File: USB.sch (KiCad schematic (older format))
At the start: 7 parts

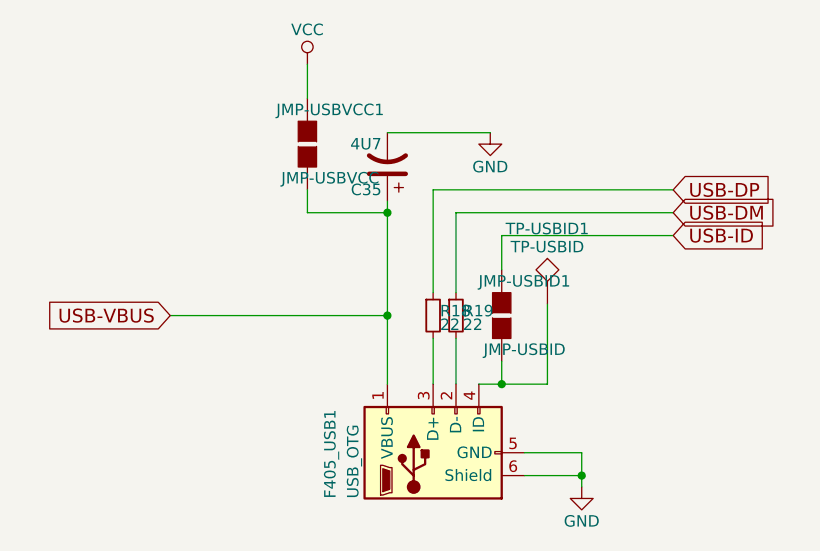
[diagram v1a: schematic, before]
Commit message: zone movement + routing of all circuits
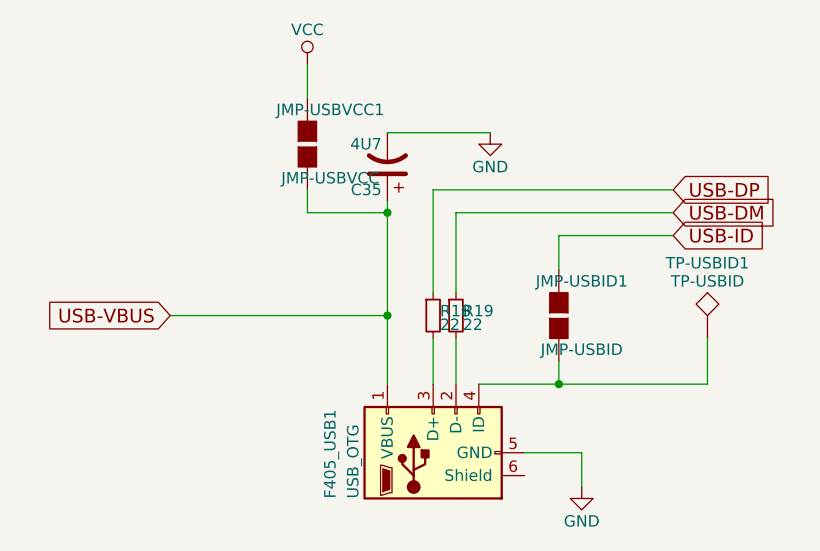
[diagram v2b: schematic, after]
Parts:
- C35: footprint (none) -> Capacitors_SMD:C_0805
- F405_USB1: footprint (none) -> gsg-modules:USB-MICROB-FCI-10103592-EXT
- JMP-USBID1, JMP-USBVCC1: footprint Connectors:GS2 -> Connect:GS2
- R18, R19: footprint (none) -> Resistors_SMD:R_0603
- TP-USBID1: footprint (none) -> Measurement_Points:Measurement_Point_Round-SMD-Pad_Small
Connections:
- net GND: no longer F405_USB1.6 (Shield)
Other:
- moved on the sheet: JMP-USBID1, TP-USBID1
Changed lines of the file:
@@
 EESchema Schematic File Version 2
 LIBS:power
-LIBS:device
 LIBS:transistors
 LIBS:conn
@@
 LIBS:sensors
 LIBS:dc-dc
+LIBS:device
 LIBS:dc26-cache
 EELAYER 25 0
@@
 $Descr A4 11693 8268
 encoding utf-8
-Sheet 5 6
+Sheet 4 6
 Title ""
 Date ""
@@
 F 0 "F405_USB1" H 5650 4750 50  0000 L CNN
 F 1 "USB_OTG" H 5650 4650 50  0000 L CNN
-F 2 "" H 6000 4250 50  0001 C CNN
+F 2 "gsg-modules:USB-MICROB-FCI-10103592-EXT" H 6000 4250 50  0001 C CNN
 F 3 "" H 6000 4250 50  0001 C CNN
 	1    5850 4300
@@
 F 0 "R18" H 5880 3720 50  0000 L CNN
 F 1 "22" H 5880 3660 50  0000 L CNN
-F 2 "" H 5850 3700 50  0001 C CNN
+F 2 "Resistors_SMD:R_0603" H 5850 3700 50  0001 C CNN
 F 3 "" H 5850 3700 50  0001 C CNN
 	1    5850 3700
@@
 F 0 "R19" H 5980 3720 50  0000 L CNN
 F 1 "22" H 5980 3660 50  0000 L CNN
-F 2 "" H 5950 3700 50  0001 C CNN
+F 2 "Resistors_SMD:R_0603" H 5950 3700 50  0001 C CNN
 F 3 "" H 5950 3700 50  0001 C CNN
 	1    5950 3700
@@
 F 0 "C35" H 5675 3150 50  0000 L CNN
 F 1 "4U7" H 5675 2950 50  0000 L CNN
-F 2 "" H 5650 3050 50  0001 C CNN
+F 2 "Capacitors_SMD:C_0805" H 5650 3050 50  0001 C CNN
 F 3 "" H 5650 3050 50  0001 C CNN
 	1    5650 3050
@@
 $EndComp
 $Comp
-L GND #PWR1248
+L GND #PWR043
 U 1 1 5B312B57
 P 6100 2900
-F 0 "#PWR1248" H 6100 2650 50  0001 C CNN
+F 0 "#PWR043" H 6100 2650 50  0001 C CNN
 F 1 "GND" H 6100 2750 50  0000 C CNN
 F 2 "" H 6100 2900 50  0001 C CNN
@@
 $EndComp
 $Comp
-L GND #PWR1249
+L GND #PWR044
 U 1 1 5B312B5D
 P 6500 4450
-F 0 "#PWR1249" H 6500 4200 50  0001 C CNN
+F 0 "#PWR044" H 6500 4200 50  0001 C CNN
 F 1 "GND" H 6500 4300 50  0000 C CNN
 F 2 "" H 6500 4450 50  0001 C CNN
@@
 L TEST TP-USBID1
 U 1 1 5B312B63
-P 6350 3650
-F 0 "TP-USBID1" H 6350 3950 50  0000 C BNN
-F 1 "TP-USBID" H 6350 3900 50  0000 C CNN
-F 2 "" H 6350 3650 50  0001 C CNN
-F 3 "" H 6350 3650 50  0001 C CNN
-	1    6350 3650
+P 7050 3800
+F 0 "TP-USBID1" H 7050 4100 50  0000 C BNN
+F 1 "TP-USBID" H 7050 4050 50  0000 C CNN
+F 2 "Measurement_Points:Measurement_Point_Round-SMD-Pad_Small" H 7050 3800 50  0001 C CNN
+F 3 "" H 7050 3800 50  0001 C CNN
+	1    7050 3800
 	1    0    0    -1
 $EndComp
@@
 L GS2 JMP-USBID1
 U 1 1 5B312B6A
-P 6150 3700
-F 0 "JMP-USBID1" H 6250 3850 50  0000 C CNN
-F 1 "JMP-USBID" H 6250 3551 50  0000 C CNN
-F 2 "Connectors:GS2" V 6224 3700 50  0001 C CNN
-F 3 "" H 6150 3700 50  0001 C CNN
-	1    6150 3700
+P 6400 3700
+F 0 "JMP-USBID1" H 6500 3850 50  0000 C CNN
+F 1 "JMP-USBID" H 6500 3551 50  0000 C CNN
+F 2 "Connect:GS2" V 6474 3700 50  0001 C CNN
+F 3 "" H 6400 3700 50  0001 C CNN
+	1    6400 3700
 	1    0    0    -1
 $EndComp
@@
 F 0 "JMP-USBVCC1" H 5400 3100 50  0000 C CNN
 F 1 "JMP-USBVCC" H 5400 2801 50  0000 C CNN
-F 2 "Connectors:GS2" V 5374 2950 50  0001 C CNN
+F 2 "Connect:GS2" V 5374 2950 50  0001 C CNN
 F 3 "" H 5300 2950 50  0001 C CNN
 	1    5300 2950
@@
 $EndComp
 $Comp
-L VCC #PWR1247
+L VCC #PWR045
 U 1 1 5B312B78
 P 5300 2600
-F 0 "#PWR1247" H 5300 2450 50  0001 C CNN
+F 0 "#PWR045" H 5300 2450 50  0001 C CNN
 F 1 "VCC" H 5300 2750 50  0000 C CNN
 F 2 "" H 5300 2600 50  0001 C CNN
@@
 $EndComp
 Wire Wire Line
-	4700 3700 5650 3700
+	5650 3700 4700 3700
 Wire Wire Line
 	5650 3200 5650 4000
@@
 	6500 4300 6500 4450
 Wire Wire Line
-	6350 4000 6350 3650
-Wire Wire Line
-	6250 4400 6500 4400
-Connection ~ 6500 4400
-Wire Wire Line
-	6150 3350 6150 3500
-Wire Wire Line
-	6050 4000 6350 4000
-Wire Wire Line
-	6150 4000 6150 3900
-Connection ~ 6150 4000
+	7050 4000 7050 3800
+Wire Wire Line
+	6400 3350 6400 3500
+Wire Wire Line
+	6050 4000 7050 4000
+Wire Wire Line
+	6400 4000 6400 3900
+Connection ~ 6400 4000
 Wire Wire Line
 	5300 3150 5300 3250
@@
 USB-ID
 Wire Wire Line
-	6150 3350 6900 3350
+	6400 3350 6900 3350
 Text GLabel 4700 3700 0    60   Input ~ 0
 USB-VBUS

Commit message: splitting led power out from 5v so that we can insert the mosfet
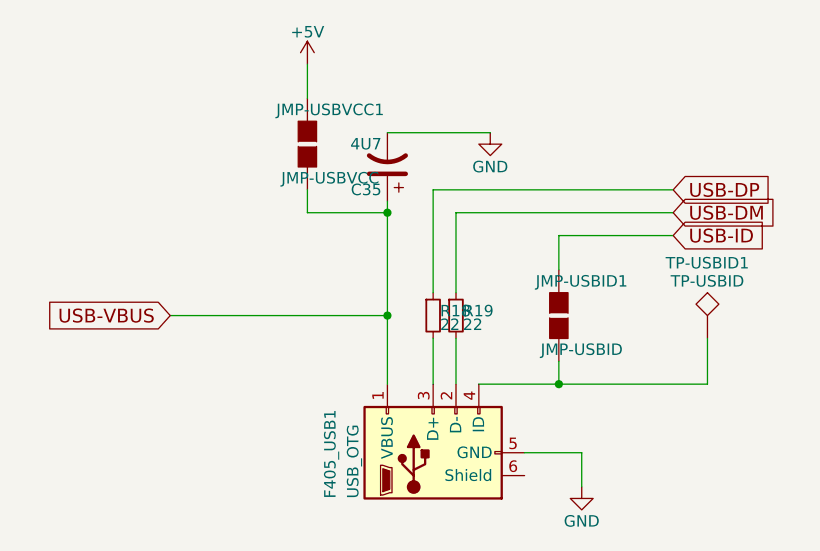
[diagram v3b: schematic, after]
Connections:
- net VCC renamed +5V
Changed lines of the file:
@@
 $EndComp
 $Comp
-L GND #PWR043
+L GND #PWR43
 U 1 1 5B312B57
 P 6100 2900
-F 0 "#PWR043" H 6100 2650 50  0001 C CNN
+F 0 "#PWR43" H 6100 2650 50  0001 C CNN
 F 1 "GND" H 6100 2750 50  0000 C CNN
 F 2 "" H 6100 2900 50  0001 C CNN
@@
 $EndComp
 $Comp
-L GND #PWR044
+L GND #PWR44
 U 1 1 5B312B5D
 P 6500 4450
-F 0 "#PWR044" H 6500 4200 50  0001 C CNN
+F 0 "#PWR44" H 6500 4200 50  0001 C CNN
 F 1 "GND" H 6500 4300 50  0000 C CNN
 F 2 "" H 6500 4450 50  0001 C CNN
@@
 F 3 "" H 5300 2950 50  0001 C CNN
 	1    5300 2950
-	1    0    0    -1
-$EndComp
-$Comp
-L VCC #PWR045
-U 1 1 5B312B78
-P 5300 2600
-F 0 "#PWR045" H 5300 2450 50  0001 C CNN
-F 1 "VCC" H 5300 2750 50  0000 C CNN
-F 2 "" H 5300 2600 50  0001 C CNN
-F 3 "" H 5300 2600 50  0001 C CNN
-	1    5300 2600
 	1    0    0    -1
 $EndComp
@@
 Wire Wire Line
 	5850 3150 6900 3150
+$Comp
+L +5V #PWR?
+U 1 1 5B114EBC
+P 5300 2600
+F 0 "#PWR?" H 5300 2450 50  0001 C CNN
+F 1 "+5V" H 5300 2740 50  0000 C CNN
+F 2 "" H 5300 2600 50  0001 C CNN
+F 3 "" H 5300 2600 50  0001 C CNN
+	1    5300 2600
+	1    0    0    -1
+$EndComp
 $EndSCHEMATC

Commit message: Footprint updates
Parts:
- C35: footprint Capacitors_SMD:C_0805 -> Capacitors_Tantalum_SMD:CP_Tantalum_Case-A_EIA-3216-18_Reflow
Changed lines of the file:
@@
 F 0 "C35" H 5675 3150 50  0000 L CNN
 F 1 "4U7" H 5675 2950 50  0000 L CNN
-F 2 "Capacitors_SMD:C_0805" H 5650 3050 50  0001 C CNN
+F 2 "Capacitors_Tantalum_SMD:CP_Tantalum_Case-A_EIA-3216-18_Reflow" H 5650 3050 50  0001 C CNN
 F 3 "" H 5650 3050 50  0001 C CNN
 	1    5650 3050
@@
 	5850 3150 6900 3150
 $Comp
-L +5V #PWR?
+L +5V #PWR42
 U 1 1 5B114EBC
 P 5300 2600
-F 0 "#PWR?" H 5300 2450 50  0001 C CNN
+F 0 "#PWR42" H 5300 2450 50  0001 C CNN
 F 1 "+5V" H 5300 2740 50  0000 C CNN
 F 2 "" H 5300 2600 50  0001 C CNN

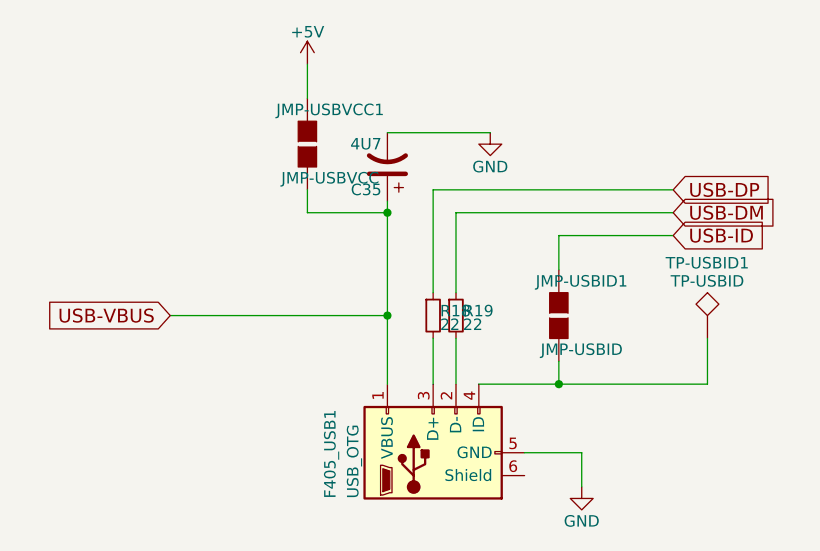
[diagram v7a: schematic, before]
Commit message: Changing tp silkscreen names
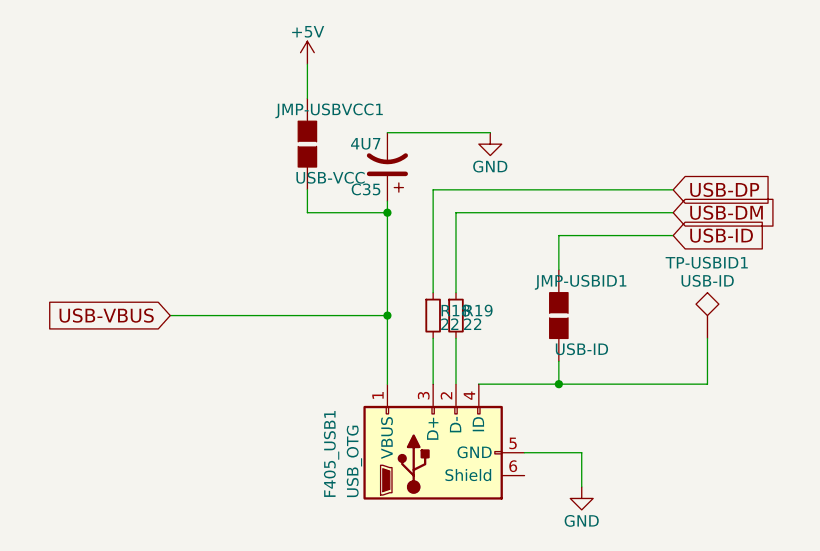
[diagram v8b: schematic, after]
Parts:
- JMP-USBID1: value JMP-USBID -> USB-ID
- JMP-USBVCC1: value JMP-USBVCC -> USB-VCC
- TP-USBID1: value TP-USBID -> USB-ID
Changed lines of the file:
@@
 $Descr A4 11693 8268
 encoding utf-8
-Sheet 4 6
+Sheet 4 7
 Title ""
 Date ""
@@
 $EndComp
 $Comp
-L GND #PWR048
+L GND #PWR44
 U 1 1 5B312B57
 P 6100 2900
-F 0 "#PWR048" H 6100 2650 50  0001 C CNN
+F 0 "#PWR44" H 6100 2650 50  0001 C CNN
 F 1 "GND" H 6100 2750 50  0000 C CNN
 F 2 "" H 6100 2900 50  0001 C CNN
@@
 $EndComp
 $Comp
-L GND #PWR049
+L GND #PWR45
 U 1 1 5B312B5D
 P 6500 4450
-F 0 "#PWR049" H 6500 4200 50  0001 C CNN
+F 0 "#PWR45" H 6500 4200 50  0001 C CNN
 F 1 "GND" H 6500 4300 50  0000 C CNN
 F 2 "" H 6500 4450 50  0001 C CNN
@@
 P 7050 3800
 F 0 "TP-USBID1" H 7050 4100 50  0000 C BNN
-F 1 "TP-USBID" H 7050 4050 50  0000 C CNN
+F 1 "USB-ID" H 7050 4050 50  0000 C CNN
 F 2 "Measurement_Points:Measurement_Point_Round-SMD-Pad_Small" H 7050 3800 50  0001 C CNN
 F 3 "" H 7050 3800 50  0001 C CNN
@@
 P 6400 3700
 F 0 "JMP-USBID1" H 6500 3850 50  0000 C CNN
-F 1 "JMP-USBID" H 6500 3551 50  0000 C CNN
+F 1 "USB-ID" H 6500 3551 50  0000 C CNN
 F 2 "Connect:GS2" V 6474 3700 50  0001 C CNN
 F 3 "" H 6400 3700 50  0001 C CNN
@@
 P 5300 2950
 F 0 "JMP-USBVCC1" H 5400 3100 50  0000 C CNN
-F 1 "JMP-USBVCC" H 5400 2801 50  0000 C CNN
+F 1 "USB-VCC" H 5400 2801 50  0000 C CNN
 F 2 "Connect:GS2" V 5374 2950 50  0001 C CNN
 F 3 "" H 5300 2950 50  0001 C CNN
@@
 	5850 3150 6900 3150
 $Comp
-L +5V #PWR050
+L +5V #PWR43
 U 1 1 5B114EBC
 P 5300 2600
-F 0 "#PWR050" H 5300 2450 50  0001 C CNN
+F 0 "#PWR43" H 5300 2450 50  0001 C CNN
 F 1 "+5V" H 5300 2740 50  0000 C CNN
 F 2 "" H 5300 2600 50  0001 C CNN
